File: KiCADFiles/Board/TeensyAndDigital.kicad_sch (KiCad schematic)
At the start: 28 parts, among them U13 SI8662BC, U14 SI8602AC

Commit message: chose all components
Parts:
- removed A1: RaspberryPi_Pico_W, Module:RaspberryPi_Pico_W_SMD_HandSolder, symbol MCU_Module:RaspberryPi_Pico_W
- removed C18, C35: 10uF, ~, symbol SuperAudioBoard-rescue:C
- added R35: 0, PCM_SparkFun-Resistor:R_0805_2012Metric, symbol SuperAudioBoard-rescue:R
- added U7: Teensy4.0, Teensy:Teensy40, symbol Teensy:Teensy4.0
- C75, C76, C77, C78: footprint ~ -> PCM_SparkFun-Capacitor:C_0603_1608Metric; MPN (none) -> CL10B104KB8NNNL
- R46, R47, R48, R49, R50, R51, R52, R53, R54, R55: footprint ~ -> PCM_SparkFun-Resistor:R_0805_2012Metric; now not fitted
- R56, R61, R62, R63, R64: footprint ~ -> PCM_SparkFun-Resistor:R_0805_2012Metric; MPN (none) -> RC0805FR-0751RL
- R57, R58, R59, R60: footprint ~ -> PCM_SparkFun-Resistor:R_0805_2012Metric; MPN (none) -> RC0805FR-072K2L
- U13: footprint (none) -> Package_SO:SOIC-16W_7.5x10.3mm_P1.27mm; MPN (none) -> SI8662BC
- U14: footprint (none) -> Package_SO:SOIC-8_3.9x4.9mm_P1.27mm; MPN (none) -> SI8602AC
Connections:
- net DGND: now also U7.1 (GND), U7.17 (GND), U7.32 (GND), U7.47 (GND)
- net T_3.3V: now also U7.16 (3V3), U7.31 (3V3), U7.49 (3V3)
- net T_ADC_DATA: now also R35.1
- net T_BCLK: now also U7.28 (21_A7_RX5_BCLK1)
- net T_CODEC_RESET: now also U7.2 (0_RX1_CRX2_CS1)
- net T_LRCLK: now also U7.27 (20_A6_TX5_LRCLK1)
- net T_SCL: now also U7.26 (19_A5_SCL0)
- net T_SCLK: now also U7.30 (23_A9_CRX1_MCLK1)
- net T_SDA: now also U7.25 (18_A4_SDA0)
- net T_VIN: now also U7.33 (VIN)
- net at R56.1: now also U7.10 (8_TX2_IN1)
- new net: R35.2, U7.9 (7_RX2_OUT1A)
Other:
- moved on the sheet: R56

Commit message: finished layout, passed DRC
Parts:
- C75, C76, C77, C78: footprint PCM_SparkFun-Capacitor:C_0603_1608Metric -> Capacitor_SMD:C_0603_1608Metric_Pad1.08x0.95mm_HandSolder
- R35, R46, R47, R48, R49, R50, R51, R52, R53, R54, R55, R56, R57, R58, R59, R60, R61, R62, R63, R64: footprint PCM_SparkFun-Resistor:R_0805_2012Metric -> Resistor_SMD:R_0805_2012Metric
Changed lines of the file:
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@@
 			)
 		)
-		(property "Footprint" "PCM_SparkFun-Resistor:R_0805_2012Metric"
+		(property "Footprint" "Resistor_SMD:R_0805_2012Metric"
 			(at 236.22 66.548 90)
 			(effects
@@
 			)
 		)
-		(property "Footprint" "PCM_SparkFun-Resistor:R_0805_2012Metric"
+		(property "Footprint" "Resistor_SMD:R_0805_2012Metric"
 			(at 187.452 101.6 90)
 			(effects
@@
 			)
 		)
-		(property "Footprint" "PCM_SparkFun-Resistor:R_0805_2012Metric"
+		(property "Footprint" "Resistor_SMD:R_0805_2012Metric"
 			(at 236.22 61.468 90)
 			(effects
@@
 			)
 		)
-		(property "Footprint" "PCM_SparkFun-Resistor:R_0805_2012Metric"
+		(property "Footprint" "Resistor_SMD:R_0805_2012Metric"
 			(at 236.22 56.388 90)
 			(effects
@@
 			)
 		)
-		(property "Footprint" "PCM_SparkFun-Resistor:R_0805_2012Metric"
+		(property "Footprint" "Resistor_SMD:R_0805_2012Metric"
 			(at 236.22 51.308 90)
 			(effects
@@
 			)
 		)
-		(property "Footprint" "PCM_SparkFun-Resistor:R_0805_2012Metric"
+		(property "Footprint" "Resistor_SMD:R_0805_2012Metric"
 			(at 49.53 58.928 90)
 			(effects
@@
 			)
 		)
-		(property "Footprint" "PCM_SparkFun-Resistor:R_0805_2012Metric"
+		(property "Footprint" "Resistor_SMD:R_0805_2012Metric"
 			(at 192.532 101.6 90)
 			(effects
@@
 			)
 		)
-		(property "Footprint" "PCM_SparkFun-Resistor:R_0805_2012Metric"
+		(property "Footprint" "Resistor_SMD:R_0805_2012Metric"
 			(at 257.302 101.6 90)
 			(effects
@@
 			)
 		)
-		(property "Footprint" "PCM_SparkFun-Resistor:R_0805_2012Metric"
+		(property "Footprint" "Resistor_SMD:R_0805_2012Metric"
 			(at 262.382 101.6 90)
 			(effects
@@
 			)
 		)
-		(property "Footprint" "PCM_SparkFun-Resistor:R_0805_2012Metric"
+		(property "Footprint" "Resistor_SMD:R_0805_2012Metric"
 			(at 73.66 178.308 90)
 			(effects
@@
 			)
 		)
-		(property "Footprint" "PCM_SparkFun-Capacitor:C_0603_1608Metric"
+		(property "Footprint" "Capacitor_SMD:C_0603_1608Metric_Pad1.08x0.95mm_HandSolder"
 			(at 202.8952 104.14 0)
 			(effects
@@
 			)
 		)
-		(property "Footprint" "PCM_SparkFun-Capacitor:C_0603_1608Metric"
+		(property "Footprint" "Capacitor_SMD:C_0603_1608Metric_Pad1.08x0.95mm_HandSolder"
 			(at 251.1552 104.14 0)
 			(effects
@@
 			)
 		)
-		(property "Footprint" "PCM_SparkFun-Capacitor:C_0603_1608Metric"
+		(property "Footprint" "Capacitor_SMD:C_0603_1608Metric_Pad1.08x0.95mm_HandSolder"
 			(at 209.2452 40.64 0)
 			(effects
@@
 			)
 		)
-		(property "Footprint" "PCM_SparkFun-Capacitor:C_0603_1608Metric"
+		(property "Footprint" "Capacitor_SMD:C_0603_1608Metric_Pad1.08x0.95mm_HandSolder"
 			(at 169.8752 40.64 0)
 			(effects
@@
 			)
 		)
-		(property "Footprint" "PCM_SparkFun-Resistor:R_0805_2012Metric"
+		(property "Footprint" "Resistor_SMD:R_0805_2012Metric"
 			(at 73.66 173.228 90)
 			(effects
@@
 			)
 		)
-		(property "Footprint" "PCM_SparkFun-Resistor:R_0805_2012Metric"
+		(property "Footprint" "Resistor_SMD:R_0805_2012Metric"
 			(at 73.66 168.148 90)
 			(effects
@@
 			)
 		)
-		(property "Footprint" "PCM_SparkFun-Resistor:R_0805_2012Metric"
+		(property "Footprint" "Resistor_SMD:R_0805_2012Metric"
 			(at 73.66 163.068 90)
 			(effects
@@
 			)
 		)
-		(property "Footprint" "PCM_SparkFun-Resistor:R_0805_2012Metric"
+		(property "Footprint" "Resistor_SMD:R_0805_2012Metric"
 			(at 73.66 157.988 90)
 			(effects
@@
 			)
 		)
-		(property "Footprint" "PCM_SparkFun-Resistor:R_0805_2012Metric"
+		(property "Footprint" "Resistor_SMD:R_0805_2012Metric"
 			(at 73.66 152.908 90)
 			(effects
@@
 			)
 		)
-		(property "Footprint" "PCM_SparkFun-Resistor:R_0805_2012Metric"
+		(property "Footprint" "Resistor_SMD:R_0805_2012Metric"
 			(at 73.66 147.828 90)
 			(effects
@@
 			)
 		)
-		(property "Footprint" "PCM_SparkFun-Resistor:R_0805_2012Metric"
+		(property "Footprint" "Resistor_SMD:R_0805_2012Metric"
 			(at 73.66 142.748 90)
 			(effects
@@
 			)
 		)
-		(property "Footprint" "PCM_SparkFun-Resistor:R_0805_2012Metric"
+		(property "Footprint" "Resistor_SMD:R_0805_2012Metric"
 			(at 73.66 137.668 90)
 			(effects
@@
 			)
 		)
-		(property "Footprint" "PCM_SparkFun-Resistor:R_0805_2012Metric"
+		(property "Footprint" "Resistor_SMD:R_0805_2012Metric"
 			(at 73.66 132.588 90)
 			(effects
@@
 			)
 		)
-		(property "Footprint" "PCM_SparkFun-Resistor:R_0805_2012Metric"
+		(property "Footprint" "Resistor_SMD:R_0805_2012Metric"
 			(at 49.53 51.308 90)
 			(effects

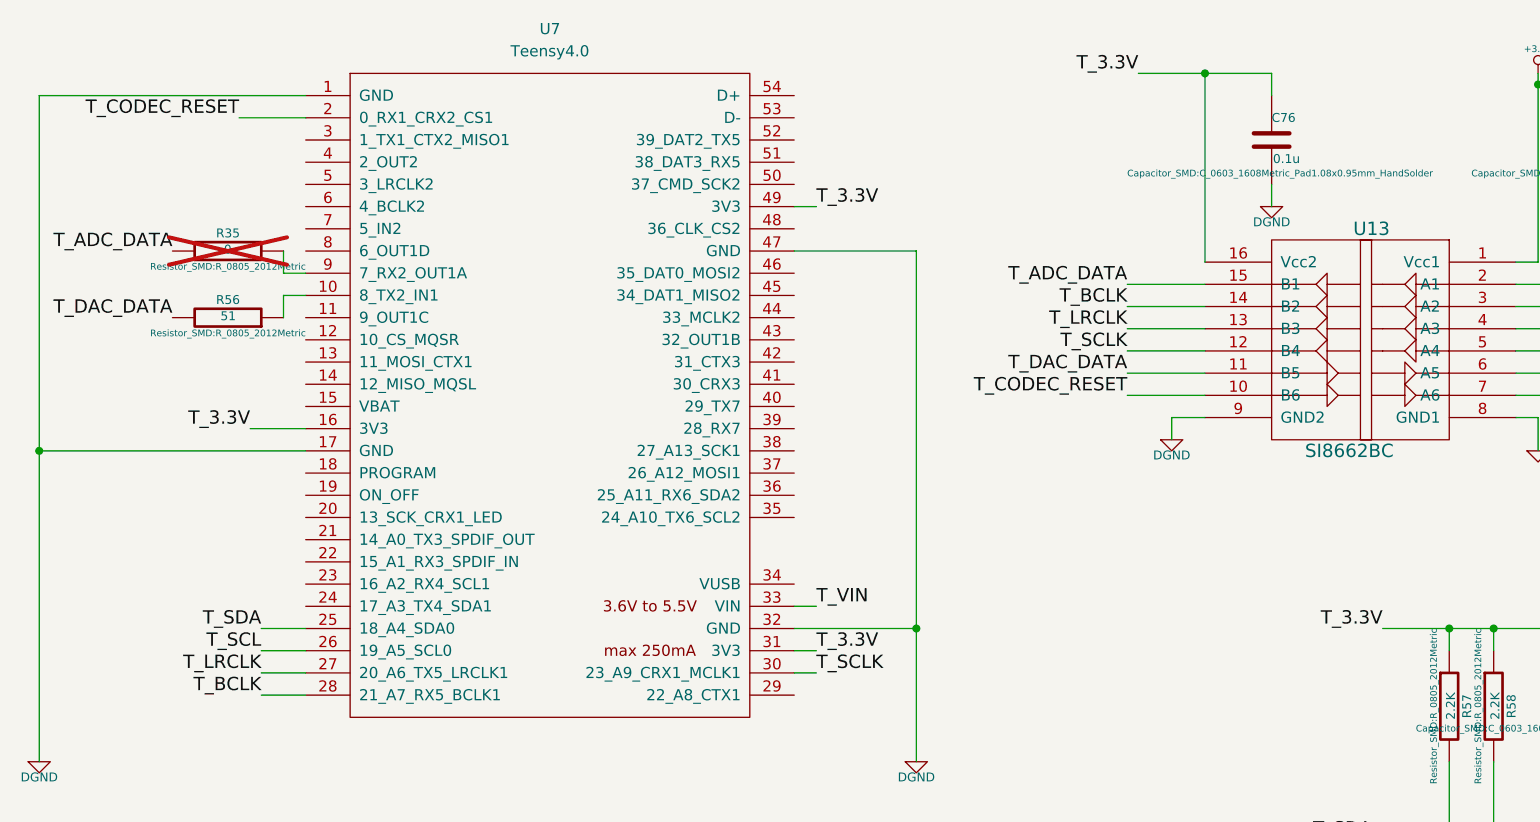
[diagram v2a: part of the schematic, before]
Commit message: added LED driver JST connector
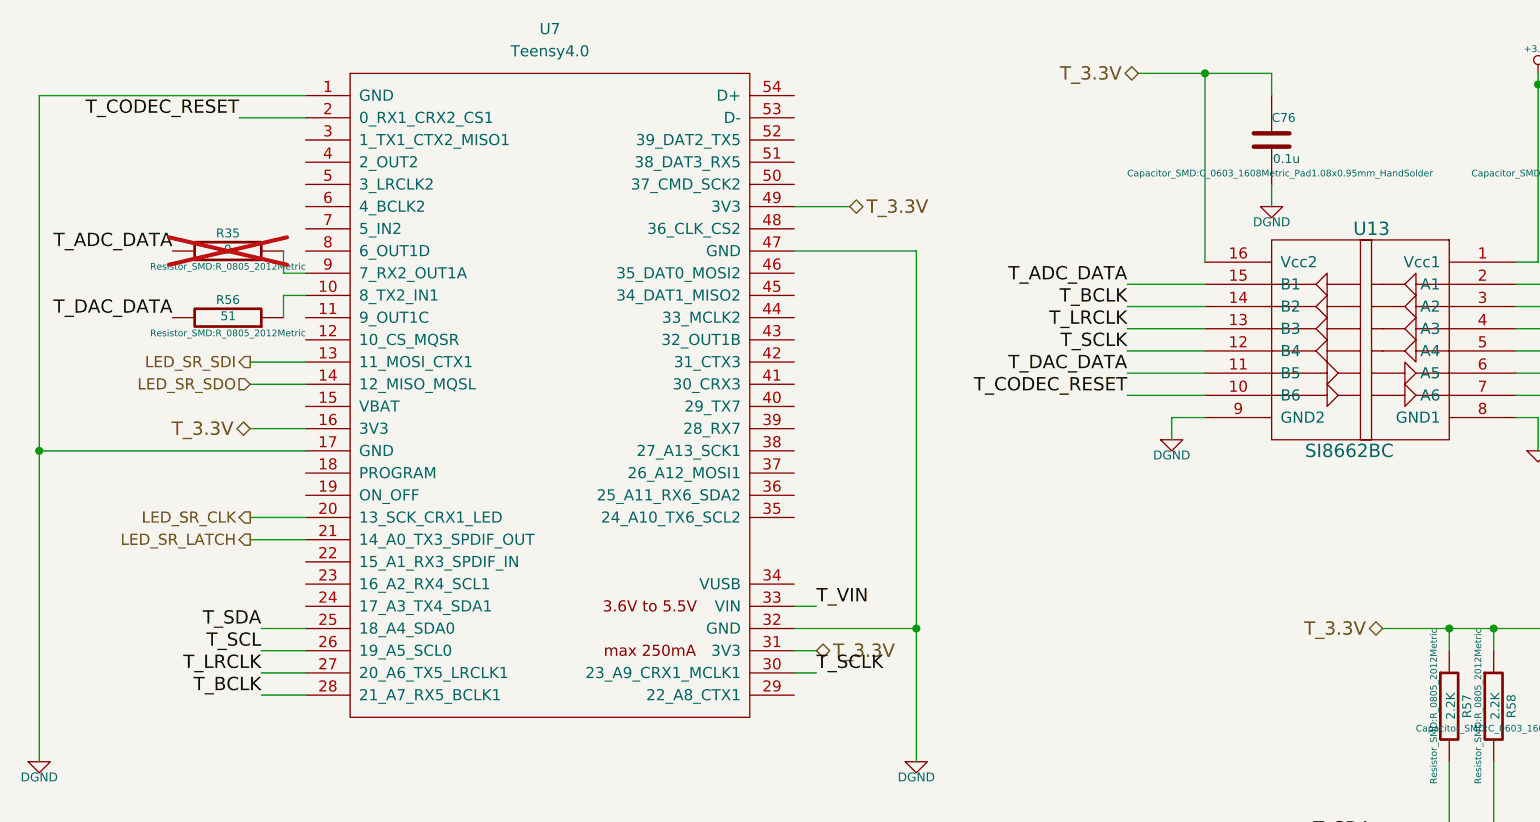
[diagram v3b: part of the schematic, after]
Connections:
- net LED_SR_SDI: now reaches U7.13 (11_MOSI_CTX1)
- net LED_SR_SDO: now reaches U7.14 (12_MISO_MQSL)
- net LED_SR_CLK: now reaches U7.20 (13_SCK_CRX1_LED)
- net LED_SR_LATCH: now reaches U7.21 (14_A0_TX3_SPDIF_OUT)
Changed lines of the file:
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@@
 	(wire
 		(pts
-			(xy 114.3 44.45) (xy 116.84 44.45)
+			(xy 114.3 44.45) (xy 120.65 44.45)
 		)
 		(stroke
@@
 	(wire
 		(pts
+			(xy 52.07 82.55) (xy 58.42 82.55)
+		)
+		(stroke
+			(width 0)
+			(type default)
+		)
+	)
+	(wire
+		(pts
 			(xy 264.16 116.84) (xy 270.51 116.84)
 		)
@@
 	(wire
 		(pts
+			(xy 52.07 62.23) (xy 58.42 62.23)
+		)
+		(stroke
+			(width 0)
+			(type default)
+		)
+	)
+	(wire
+		(pts
 			(xy 199.39 30.48) (xy 199.39 50.8)
 		)
@@
 	(wire
 		(pts
+			(xy 52.07 80.01) (xy 58.42 80.01)
+		)
+		(stroke
+			(width 0)
+			(type default)
+		)
+	)
+	(wire
+		(pts
 			(xy 264.16 107.95) (xy 264.16 116.84)
 		)
@@
 		(pts
 			(xy 201.93 92.71) (xy 201.93 95.25)
+		)
+		(stroke
+			(width 0)
+			(type default)
+		)
+	)
+	(wire
+		(pts
+			(xy 52.07 64.77) (xy 58.42 64.77)
 		)
 		(stroke
@@
 		)
 	)
-	(label "T_3.3V"
-		(at 116.84 44.45 0)
-		(effects
-			(font
-				(size 1.524 1.524)
-			)
-			(justify left bottom)
-		)
-	)
 	(label "T_BCLK"
 		(at 152.4 55.88 180)
@@
 		)
 	)
-	(label "T_3.3V"
-		(at 116.84 95.25 0)
-		(effects
-			(font
-				(size 1.524 1.524)
-			)
-			(justify left bottom)
-		)
-	)
-	(label "T_3.3V"
-		(at 153.67 29.21 180)
-		(effects
-			(font
-				(size 1.524 1.524)
-			)
-			(justify right bottom)
-		)
-	)
 	(label "T_SDA"
 		(at 180.34 116.84 180)
@@
 		)
 	)
-	(label "T_3.3V"
-		(at 181.61 92.71 180)
-		(effects
-			(font
-				(size 1.524 1.524)
-			)
-			(justify right bottom)
-		)
-	)
 	(label "C_RESET"
 		(at 227.33 74.93 180)
@@
 		)
 	)
-	(label "T_3.3V"
-		(at 52.07 69.85 180)
-		(effects
-			(font
-				(size 1.524 1.524)
-			)
-			(justify right bottom)
-		)
-	)
 	(label "C_DAC_DATA"
 		(at 95.25 156.21 0)
@@
 			)
 			(justify right bottom)
+		)
+	)
+	(hierarchical_label "T_3.3V"
+		(shape bidirectional)
+		(at 116.84 95.25 0)
+		(effects
+			(font
+				(size 1.524 1.524)
+			)
+			(justify left)
 		)
 	)
@@
 		)
 	)
+	(hierarchical_label "LED_SR_SDO"
+		(shape input)
+		(at 52.07 64.77 180)
+		(effects
+			(font
+				(size 1.27 1.27)
+			)
+			(justify right)
+		)
+	)
+	(hierarchical_label "LED_SR_CLK"
+		(shape output)
+		(at 52.07 80.01 180)
+		(effects
+			(font
+				(size 1.27 1.27)
+			)
+			(justify right)
+		)
+	)
+	(hierarchical_label "T_3.3V"
+		(shape bidirectional)
+		(at 181.61 92.71 180)
+		(effects
+			(font
+				(size 1.524 1.524)
+			)
+			(justify right)
+		)
+	)
 	(hierarchical_label "ADC_DATA"
 		(shape input)
@@
 		)
 	)
+	(hierarchical_label "LED_SR_SDI"
+		(shape output)
+		(at 52.07 62.23 180)
+		(effects
+			(font
+				(size 1.27 1.27)
+			)
+			(justify right)
+		)
+	)
+	(hierarchical_label "T_3.3V"
+		(shape bidirectional)
+		(at 120.65 44.45 0)
+		(effects
+			(font
+				(size 1.524 1.524)
+			)
+			(justify left)
+		)
+	)
+	(hierarchical_label "T_3.3V"
+		(shape bidirectional)
+		(at 52.07 69.85 180)
+		(effects
+			(font
+				(size 1.524 1.524)
+			)
+			(justify right)
+		)
+	)
 	(hierarchical_label "SDA"
 		(shape bidirectional)
@@
 		)
 	)
+	(hierarchical_label "LED_SR_LATCH"
+		(shape output)
+		(at 52.07 82.55 180)
+		(effects
+			(font
+				(size 1.27 1.27)
+			)
+			(justify right)
+		)
+	)
 	(hierarchical_label "BCLK"
 		(shape bidirectional)
@@
 		)
 	)
+	(hierarchical_label "T_3.3V"
+		(shape bidirectional)
+		(at 153.67 29.21 180)
+		(effects
+			(font
+				(size 1.524 1.524)
+			)
+			(justify right)
+		)
+	)
